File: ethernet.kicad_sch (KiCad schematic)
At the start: 39 parts, among them U1 MPFS250T-FCVG484, U16 DP83867ISRGZR

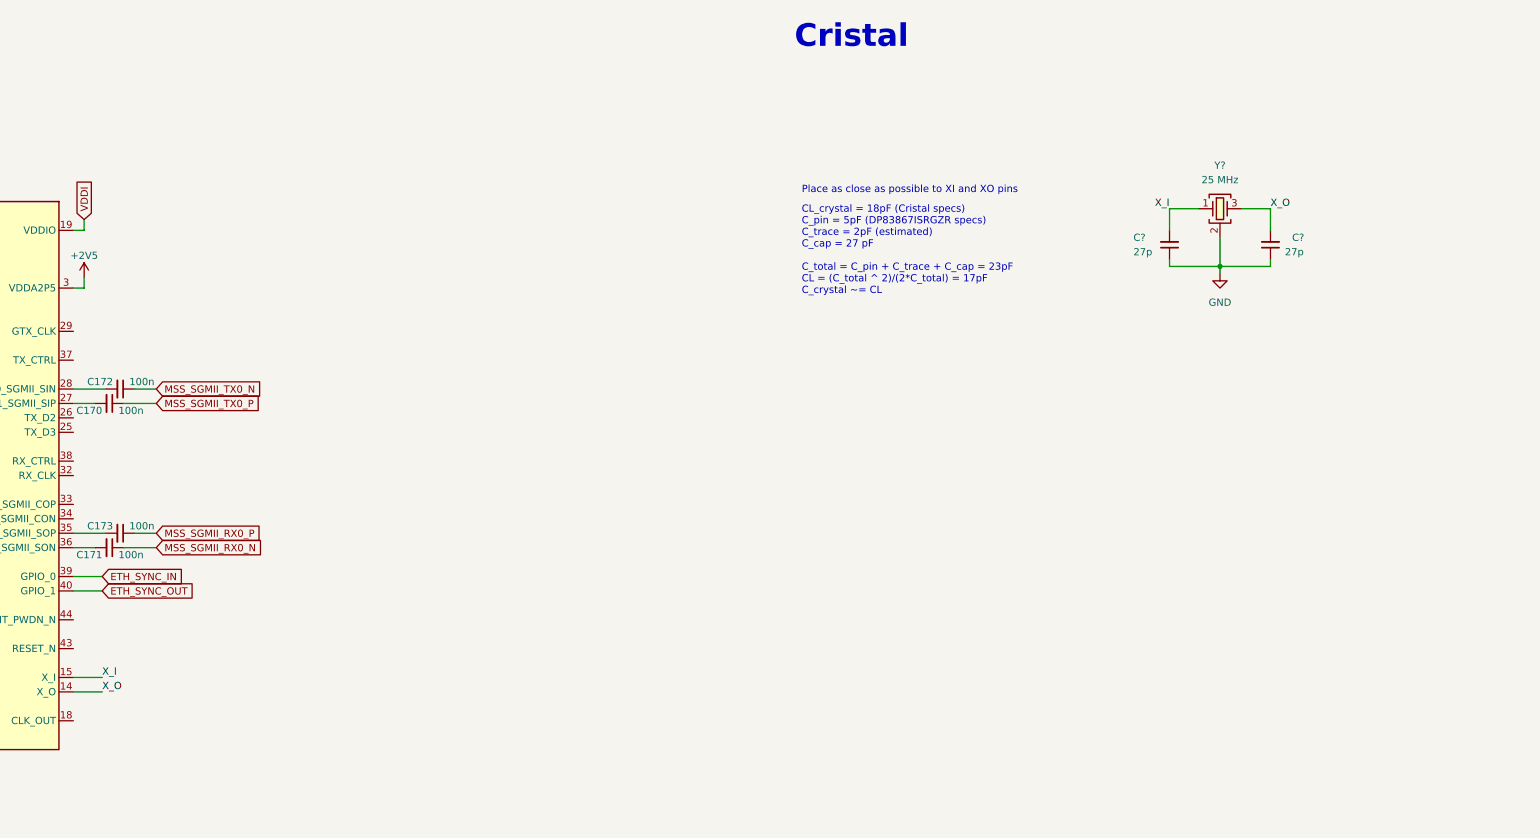
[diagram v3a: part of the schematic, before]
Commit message: [#54442] Add X_0 0R resistor
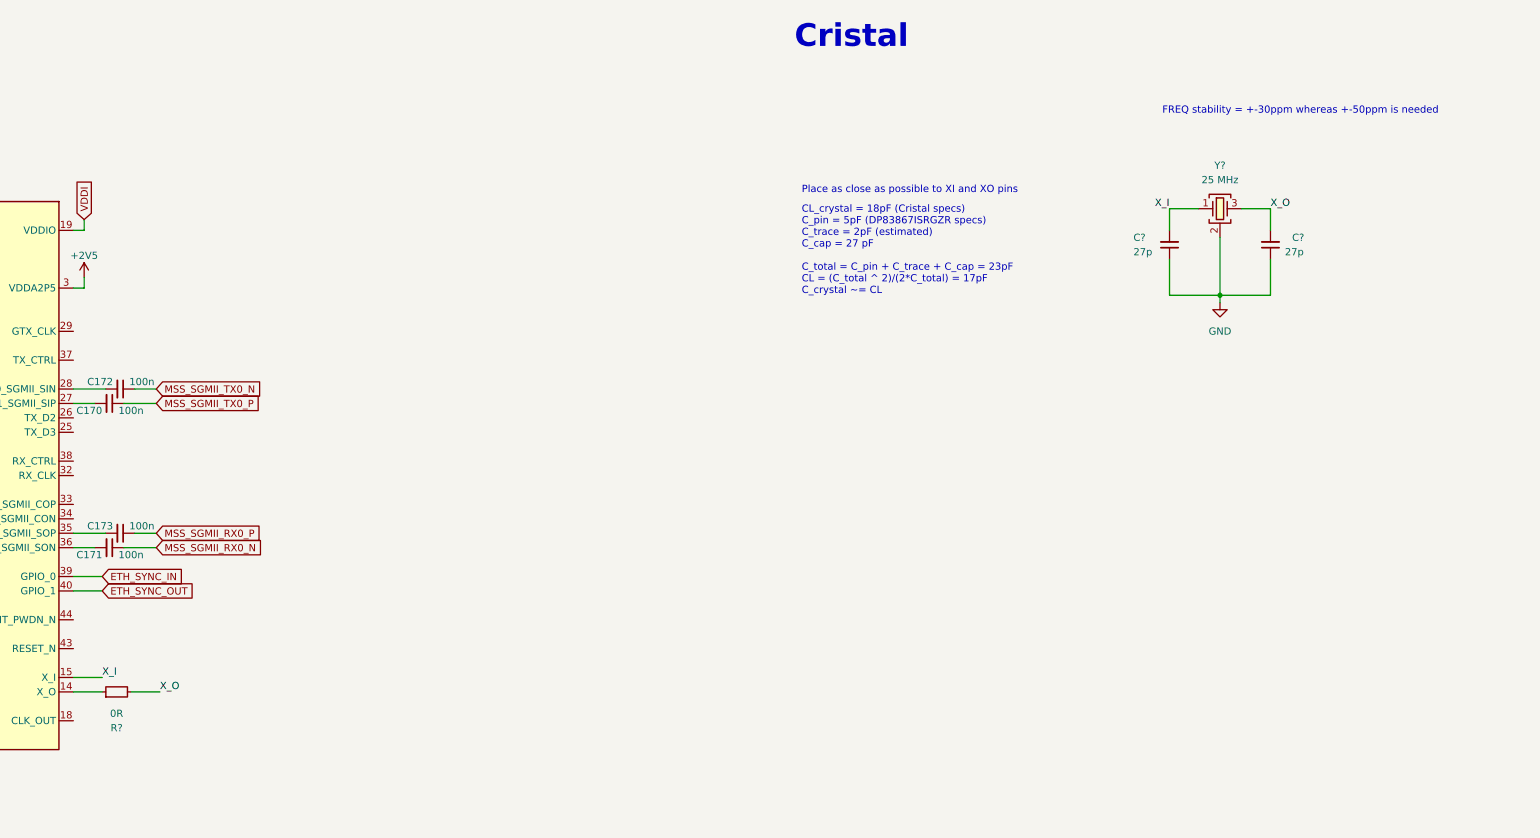
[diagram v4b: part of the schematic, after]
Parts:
- added R?: R_0R_0201, antmicro-footprints:R_0201, symbol antmicroResistorsmisc:R_0R_0201
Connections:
- net X_O: now also R?.2; no longer U16.14 (X_O)
- new net: R?.1, U16.14 (X_O)
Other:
- note added: "FREQ stability = +-30ppm whereas +-50ppm is needed"
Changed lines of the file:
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@@
   (junction (at 104.14 196.85) (diameter 0) (color 0 0 0 0)
   )
-  (junction (at 323.85 60.96) (diameter 0) (color 0 0 0 0)
+  (junction (at 323.85 66.04) (diameter 0) (color 0 0 0 0)
   )
   (junction (at 104.14 215.9) (diameter 0) (color 0 0 0 0)
@@
     (stroke (width 0) (type default) (color 0 0 0 0))
   )
+  (wire (pts (xy 314.96 59.69) (xy 314.96 66.04))
+    (stroke (width 0) (type default) (color 0 0 0 0))
+  )
   (wire (pts (xy 62.23 190.5) (xy 62.23 191.77))
     (stroke (width 0) (type default) (color 0 0 0 0))
@@
     (stroke (width 0) (type default) (color 0 0 0 0))
   )
-  (wire (pts (xy 323.85 55.88) (xy 323.85 60.96))
-    (stroke (width 0) (type default) (color 0 0 0 0))
-  )
   (wire (pts (xy 138.43 271.78) (xy 138.43 272.415))
     (stroke (width 0) (type default) (color 0 0 0 0))
@@
     (stroke (width 0) (type default) (color 0 0 0 0))
   )
-  (wire (pts (xy 314.96 60.96) (xy 323.85 60.96))
+  (wire (pts (xy 314.96 66.04) (xy 323.85 66.04))
     (stroke (width 0) (type default) (color 0 0 0 0))
   )
@@
     (stroke (width 0) (type default) (color 0 0 0 0))
   )
-  (wire (pts (xy 323.85 60.96) (xy 332.74 60.96))
+  (wire (pts (xy 323.85 66.04) (xy 332.74 66.04))
     (stroke (width 0) (type default) (color 0 0 0 0))
   )
@@
     (stroke (width 0) (type default) (color 0 0 0 0))
   )
-  (wire (pts (xy 323.85 60.96) (xy 323.85 62.23))
+  (wire (pts (xy 323.85 66.04) (xy 323.85 67.31))
     (stroke (width 0) (type default) (color 0 0 0 0))
   )
@@
     (stroke (width 0) (type default) (color 0 0 0 0))
   )
+  (wire (pts (xy 323.85 55.88) (xy 323.85 66.04))
+    (stroke (width 0) (type default) (color 0 0 0 0))
+  )
+  (wire (pts (xy 132.08 135.89) (xy 137.16 135.89))
+    (stroke (width 0) (type default) (color 0 0 0 0))
+  )
   (wire (pts (xy 132.08 265.43) (xy 132.08 266.065))
     (stroke (width 0) (type default) (color 0 0 0 0))
@@
     (stroke (width 0) (type default) (color 0 0 0 0))
   )
-  (wire (pts (xy 332.74 59.69) (xy 332.74 60.96))
+  (wire (pts (xy 332.74 59.69) (xy 332.74 66.04))
     (stroke (width 0) (type default) (color 0 0 0 0))
   )
@@
     (stroke (width 0) (type default) (color 0 0 0 0))
   )
-  (wire (pts (xy 314.96 59.69) (xy 314.96 60.96))
-    (stroke (width 0) (type default) (color 0 0 0 0))
-  )
   (wire (pts (xy 132.08 189.865) (xy 138.43 189.865))
     (stroke (width 0) (type default) (color 0 0 0 0))
@@
     (effects (font (size 4 4) (thickness 0.8) bold) (justify left bottom))
   )
+  (text "FREQ stability = +-30ppm whereas +-50ppm is needed"
+    (at 313.69 34.29 0)
+    (effects (font (size 1.27 1.27)) (justify left bottom))
+  )
   (text "Place close\nto pin 6" (at 135.89 208.28 0)
     (effects (font (size 1.27 1.27)) (justify left bottom))
@@
     (effects (font (size 1.27 1.27)) (justify right bottom))
   )
-  (label "X_O" (at 127 135.89 0)
+  (label "X_O" (at 137.16 135.89 0)
     (effects (font (size 1.27 1.27)) (justify left bottom))
   )
@@
     (pin "2")
   )
-  (symbol (lib_id "antmicropower:GND") (at 323.85 62.23 0) (unit 1)
+  (symbol (lib_id "antmicropower:GND") (at 323.85 67.31 0) (unit 1)
     (in_bom yes) (on_board yes) (fields_autoplaced)
-    (property "Reference" "#PWR?" (id 0) (at 332.74 64.77 0)
+    (property "Reference" "#PWR?" (id 0) (at 332.74 69.85 0)
       (effects (font (size 1.27 1.27) (thickness 0.15)) (justify left bottom) hide)
     )
-    (property "Value" "GND" (id 1) (at 323.85 67.31 0)
+    (property "Value" "GND" (id 1) (at 323.85 72.39 0)
       (effects (font (size 1.27 1.27) (thickness 0.15)))
     )
-    (property "Footprint" "" (id 2) (at 332.74 69.85 0)
+    (property "Footprint" "" (id 2) (at 332.74 74.93 0)
       (effects (font (size 1.27 1.27) (thickness 0.15)) (justify left bottom) hide)
     )
-    (property "Datasheet" "" (id 3) (at 332.74 74.93 0)
+    (property "Datasheet" "" (id 3) (at 332.74 80.01 0)
       (effects (font (size 1.27 1.27) (thickness 0.15)) (justify left bottom) hide)
     )
-    (property "Author" "Antmicro" (id 4) (at 332.74 69.85 0)
+    (property "Author" "Antmicro" (id 4) (at 332.74 74.93 0)
       (effects (font (size 1.27 1.27) (thickness 0.15)) (justify left bottom) hide)
     )
-    (property "License" "Apache-2.0" (id 5) (at 332.74 72.39 0)
+    (property "License" "Apache-2.0" (id 5) (at 332.74 77.47 0)
       (effects (font (size 1.27 1.27) (thickness 0.15)) (justify left bottom) hide)
     )
@@
     (pin "1")
   )
+  (symbol (lib_id "antmicroResistorsmisc:R_0R_0201") (at 127 135.89 0) (mirror x) (unit 1)
+    (in_bom yes) (on_board yes)
+    (property "Reference" "R?" (id 0) (at 129.54 142.24 0)
+      (effects (font (size 1.27 1.27) (thickness 0.15)))
+    )
+    (property "Value" "R_0R_0201" (id 1) (at 147.32 123.19 0)
+      (effects (font (size 1.27 1.27) (thickness 0.15)) (justify left bottom) hide)
+    )
+    (property "Footprint" "antmicro-footprints:R_0201" (id 2) (at 147.32 120.65 0)
+      (effects (font (size 1.27 1.27) (thickness 0.15)) (justify left bottom) hide)
+    )
+    (property "Datasheet" "https://www.bourns.com/docs/product-datasheets/cr.pdf" (id 3) (at 147.32 118.11 0)
+      (effects (font (size 1.27 1.27) (thickness 0.15)) (justify left bottom) hide)
+    )
+    (property "MPN" "CR0201-FX-0R00GLF" (id 4) (at 147.32 115.57 0)
+      (effects (font (size 1.27 1.27) (thickness 0.15)) (justify left bottom) hide)
+    )
+    (property "Manufacturer" "Bourns" (id 5) (at 147.32 113.03 0)
+      (effects (font (size 1.27 1.27) (thickness 0.15)) (justify left bottom) hide)
+    )
+    (property "License" "Apache-2.0" (id 6) (at 147.32 110.49 0)
+      (effects (font (size 1.27 1.27) (thickness 0.15)) (justify left bottom) hide)
+    )
+    (property "Author" "Antmicro" (id 7) (at 147.32 107.95 0)
+      (effects (font (size 1.27 1.27) (thickness 0.15)) (justify left bottom) hide)
+    )
+    (property "Val" "0R" (id 8) (at 129.54 139.7 0)
+      (effects (font (size 1.27 1.27) (thickness 0.15)))
+    )
+    (property "Tolerance" "1%" (id 9) (at 147.32 125.73 0)
+      (effects (font (size 1.27 1.27)) (justify left bottom) hide)
+    )
+    (pin "1")
+    (pin "2")
+  )
   (symbol (lib_id "antmicropower:+2V5") (at 62.23 209.55 0) (unit 1)

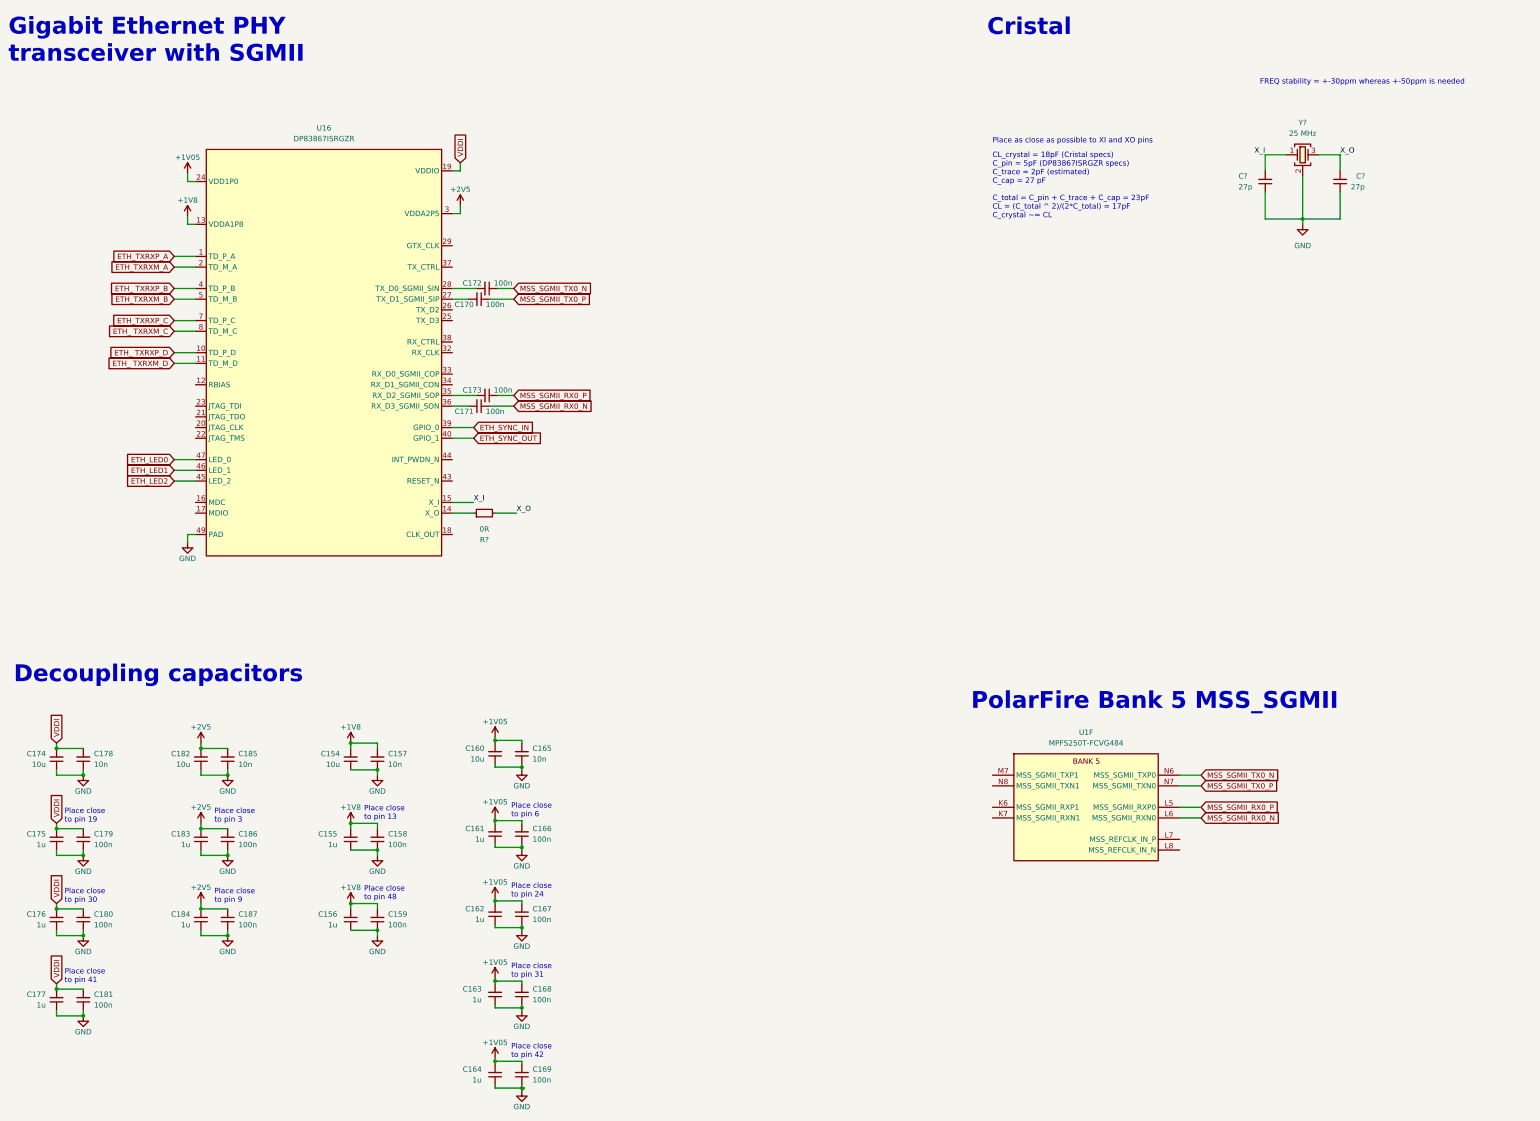
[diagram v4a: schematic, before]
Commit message: [#54442] Add SGMII routing guidelines
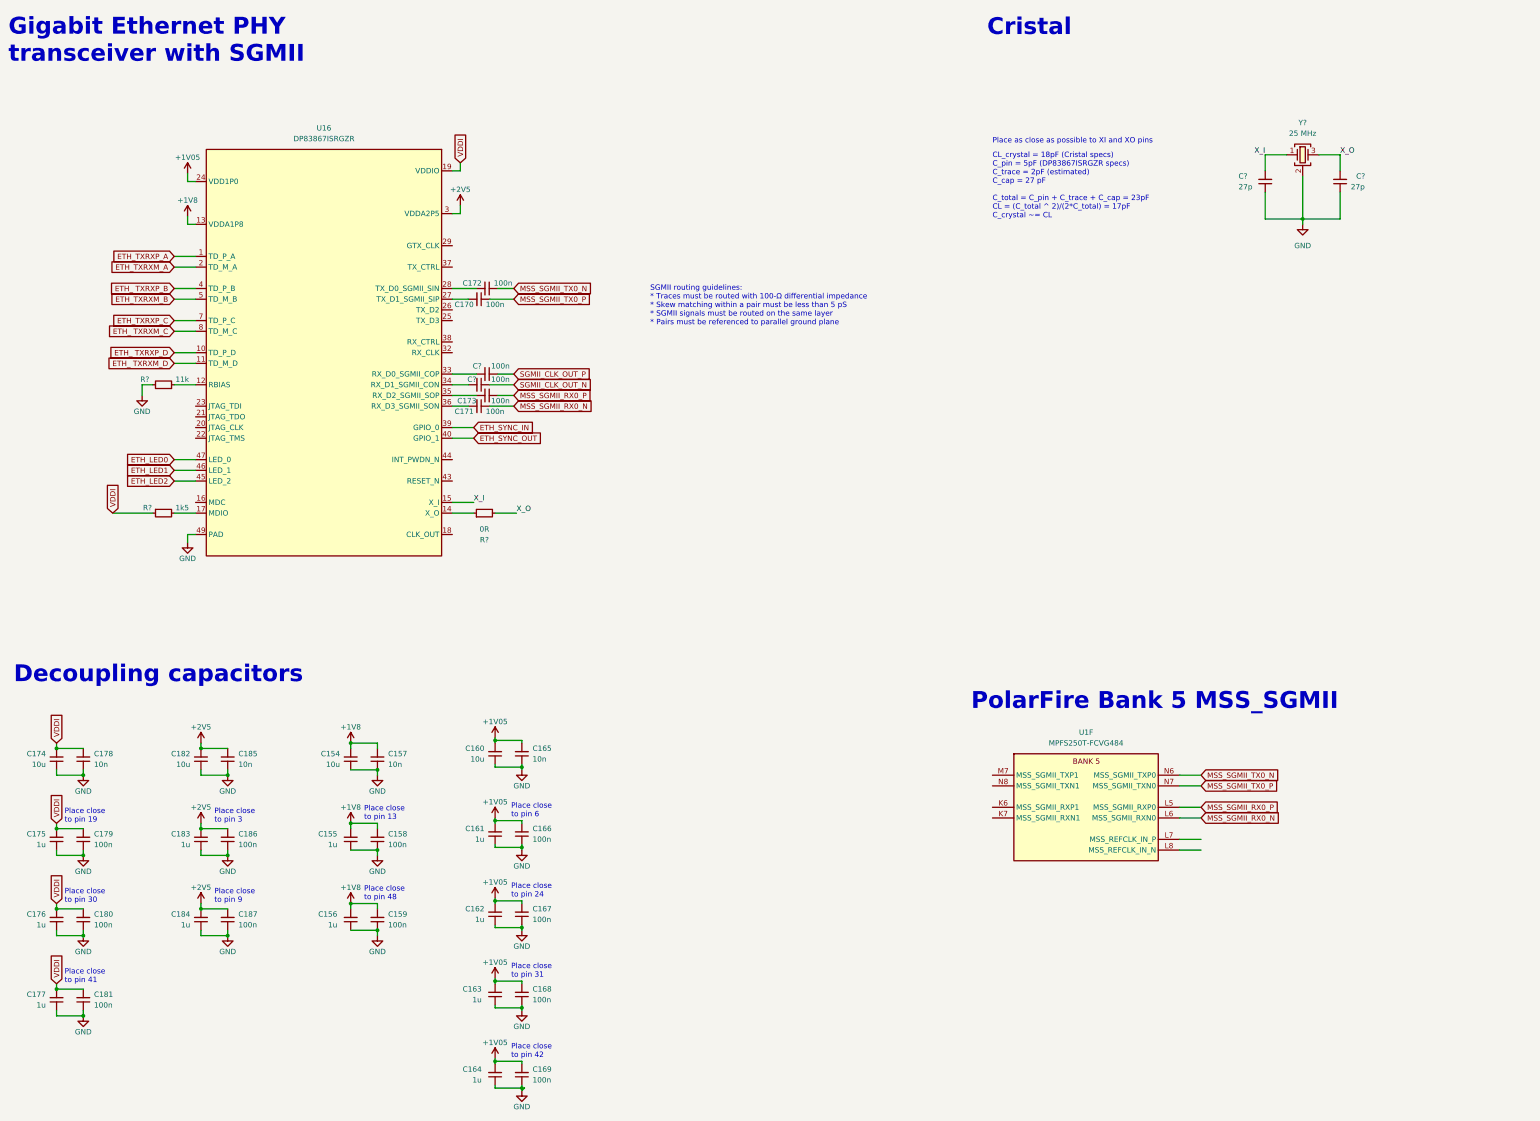
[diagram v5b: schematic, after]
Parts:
- added C? (x2): C_100n_0402, antmicro-footprints:C_0402_1005Metric, symbol antmicroCapacitors0402:C_100n_0402
- added R?: R_11k_0402, antmicro-footprints:R_0402_1005Metric, symbol antmicroResistors0402:R_11k_0402
- added R?: R_1k5_0402, antmicro-footprints:R_0402_1005Metric, symbol antmicroResistors0402:R_1k5_0402
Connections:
- net GND: now also R?.2
- net VDDI: now also R?.1
- net at U16.12 (RBIAS): now also R?.1
- net at U16.17 (MDIO): now also R?.2
- net at U16.33 (RX_D0_SGMII_COP): now also C?.2
- net at U16.34 (RX_D1_SGMII_CON): now also C?.2
- new net SGMII_CLK_OUT_N: C?.1
- new net SGMII_CLK_OUT_P: C?.1
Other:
- note added: "SGMII routing guidelines: * Traces must be routed with 100-Ω differential impedance * Skew matching within a pair must be less than 5 pS * SGMII signals must be routed on the same layer * Pairs must be referenced to parallel ground plane"
- note removed: "FREQ stability = +-30ppm whereas +-50ppm is needed"

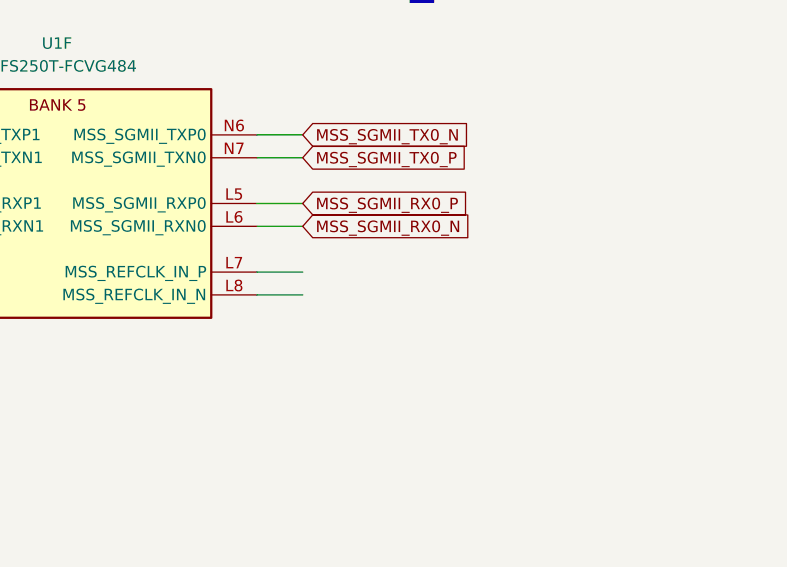
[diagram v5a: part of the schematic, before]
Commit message: [#54442] Connect SGMII reference clock
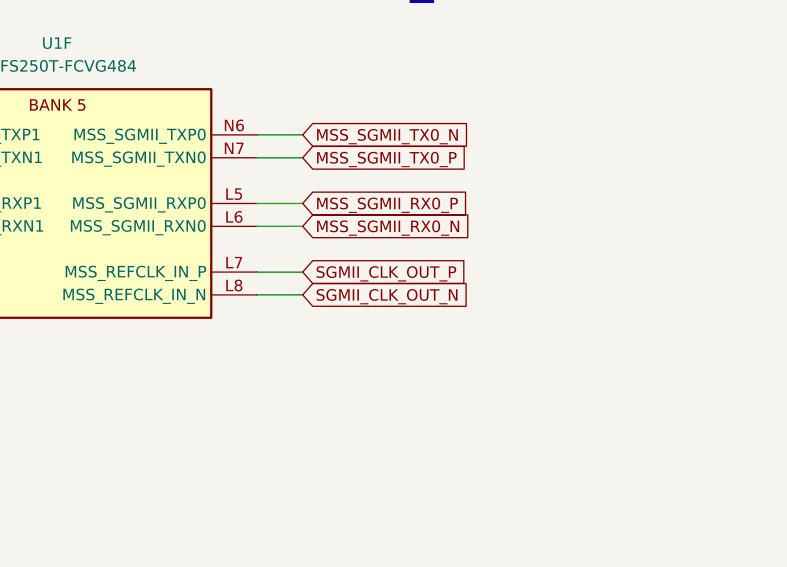
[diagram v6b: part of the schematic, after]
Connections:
- net SGMII_CLK_OUT_N: now also U1.L8 (MSS_REFCLK_IN_N)
- net SGMII_CLK_OUT_P: now also U1.L7 (MSS_REFCLK_IN_P)
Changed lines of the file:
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@@
+    )
+  )
+  (global_label "SGMII_CLK_OUT_N" (shape input) (at 299.72 215.9 0) (fields_autoplaced)
+    (effects (font (size 1.27 1.27)) (justify left))
+    (property "Intersheet References" "${INTERSHEET_REFS}" (id 0) (at 318.7036 215.8206 0)
+      (effects (font (size 1.27 1.27)) (justify left) hide)
     )
   )
@@
       (effects (font (size 1.27 1.27)) (justify left) hide)
     )
+  )
+  (global_label "SGMII_CLK_OUT_P" (shape input) (at 299.72 213.36 0) (fields_autoplaced)
+    (effects (font (size 1.27 1.27)) (justify left))
+    (property "Intersheet References" "${INTERSHEET_REFS}" (id 0) (at 318.6431 213.2806 0)
+      (effects (font (size 1.27 1.27)) (justify left) hide)
+    )
